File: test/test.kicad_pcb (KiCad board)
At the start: 2 copper layers, 20.3 x 20.3 mm, 4 parts

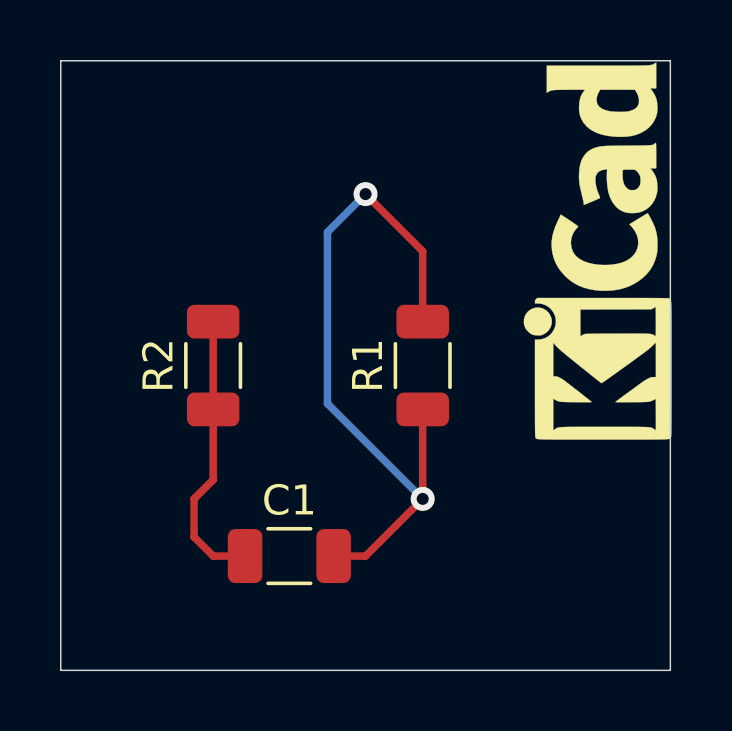
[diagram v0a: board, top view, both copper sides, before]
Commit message: add more things to test exports
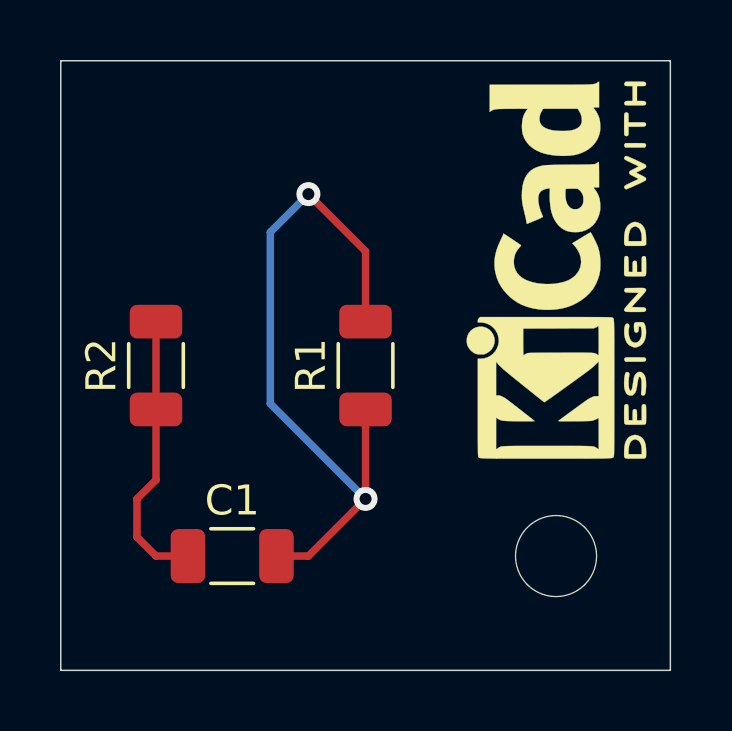
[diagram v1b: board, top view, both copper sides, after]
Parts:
- added H1: MountingHole, MountingHole:MountingHole_2.7mm, F.Cu at (135.9, 105.4)
- C1: value C -> 100nF
- LOGO1: value Logo_Open_Hardware_Large -> Logo_Open_Hardware_Small; footprint Symbol:KiCad-Logo_5mm_SilkScreen -> Symbol:KiCad-Logo2_5mm_SilkScreen
- moved LOGO1 2.01 mm to (135.9, 95.9)
- moved C1 1.91 mm to (125.1, 105.4)
- moved R1 1.91 mm to (129.5, 99.1)
- moved R2 1.90 mm to (122.6, 99.1)
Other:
- board text added: "Lorem ipsum dolor sit amet, consectetur adipiscing elit, sed do eiusmod tempor incididunt ut labore et dolore magna aliqua. Ut enim ad minim veniam, quis nostrud exercitation ullamco laboris nisi ut aliquip ex ea commodo consequat. Duis aute irure dolor in reprehenderit in voluptate velit esse cillum dolore eu fugiat nulla pariatur. Excepteur sint occaecat cupidatat non proident, sunt in culpa qu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"

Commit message: changed test project
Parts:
- removed H1: MountingHole, MountingHole:MountingHole_2.7mm
- added C2: 100nF, Capacitor_SMD:C_1206_3216Metric, F.Cu at (134.6, 104.8)
- added U1: TLV70233_SOT23-5, Package_TO_SOT_SMD:SOT-23-5, F.Cu at (129.5, 104.8)
- added U2: FT230XQ, Package_DFN_QFN:QFN-16-1EP_4x4mm_P0.65mm_EP2.1x2.1mm, F.Cu at (124.5, 95.9)
- R1, R2: value 100 -> R; footprint Resistor_SMD:R_1206_3216Metric -> Resistor_SMD:R_0805_2012Metric
- moved R2 8.47 mm to (130.8, 97.2), turned to 0 degrees
- moved R1 7.10 mm to (130.8, 92.1), turned to 0 degrees
- moved C1 1.42 mm to (123.8, 104.8), turned to 90 degrees
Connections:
- C1 pad 2: Net-(C1-Pad2) -> GND
- R1 pad 1: Net-(C1-Pad2) -> +3V3
- R1 pad 2: Net-(C1-Pad2) -> GND
- R2 pad 1: Net-(C1-Pad1) -> +3V3
- R2 pad 2: Net-(C1-Pad1) -> GND
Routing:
- net +3V3: track 0.00 -> 33.4 mm
- net Net-(C1-Pad2): track 24.0 -> 0.00 mm, vias 2 -> 0
- net GND: track 0.00 -> 4.44 mm
- net Net-(C1-Pad1): track 10.1 -> 7.92 mm
- added copper zone on F.Cu, net GND
